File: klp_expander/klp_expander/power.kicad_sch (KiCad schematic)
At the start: 20 parts, among them U2 LM22678TJ-5, U4 AMS1117-3.3

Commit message: update schematics
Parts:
- added C40, C41: 100n, Capacitor_SMD:C_0402_1005Metric, symbol Device:C_Small
- added C46: 470p, Capacitor_SMD:C_0603_1608Metric, symbol Device:C
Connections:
- net +24V: now also C40.2, C41.2
- net GND: now also C40.1, C41.1, C46.1
- new net GNDS: C46.2

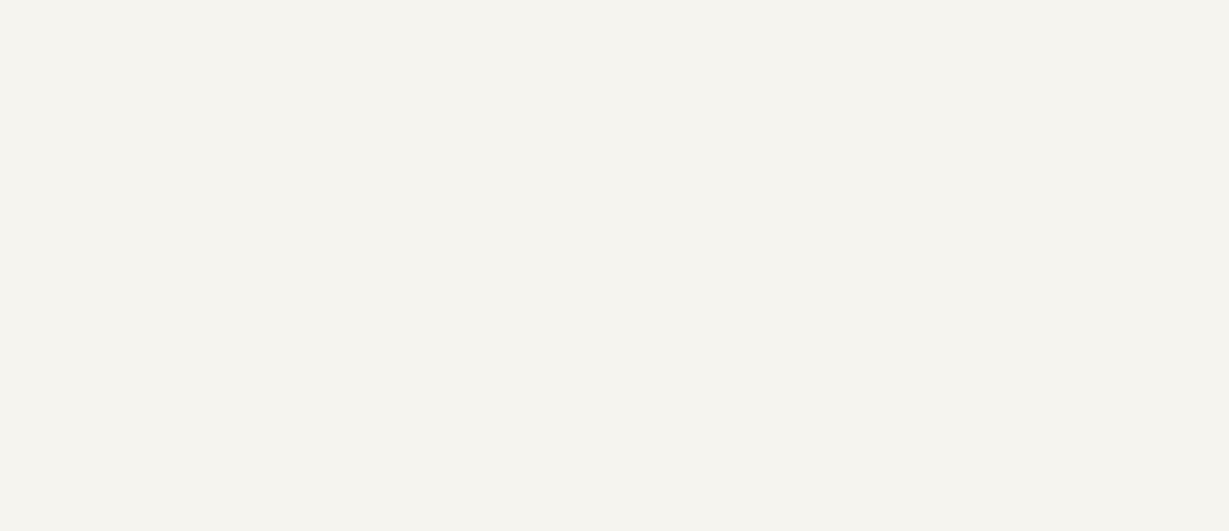
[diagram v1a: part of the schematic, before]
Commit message: feat: merge middle mcu into klp expander. both projects will be merged and will get a new name
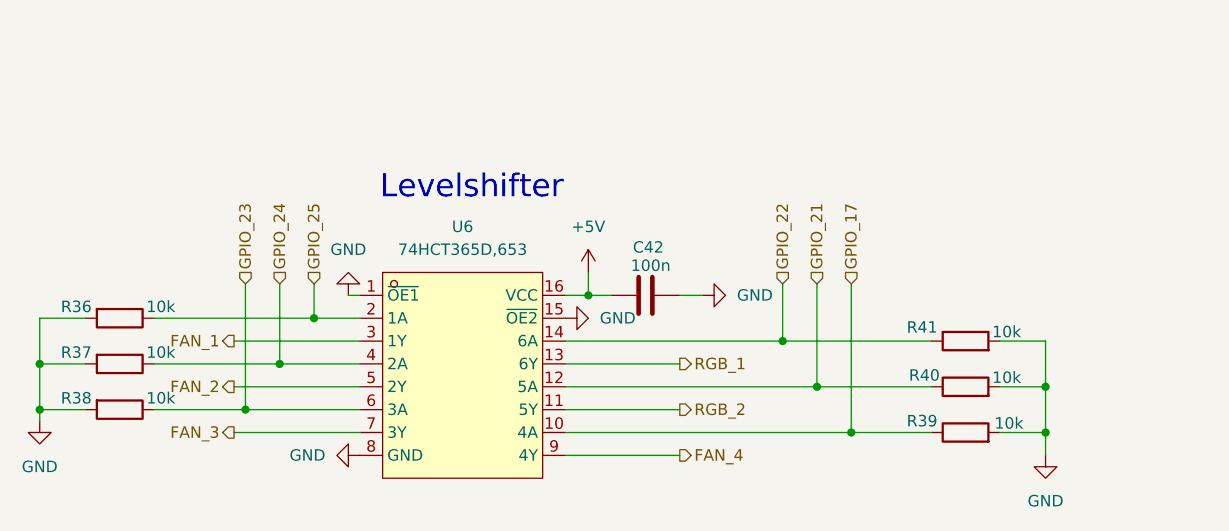
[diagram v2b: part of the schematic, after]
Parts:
- added C42: 100n, Capacitor_SMD:C_0402_1005Metric, symbol Device:C
- added R36, R37, R38, R39, R40, R41: 10k, Resistor_SMD:R_0402_1005Metric, symbol Device:R
- added U6: 74HCT365D,653, :SOP-16_L10.0-W3.9-P1.27-LS6.0-BL, symbol LCSC:74HCT365D,653
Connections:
- net +5V: now also C42.1, U6.16 (VCC)
- net GND: now also C42.2, R36.2, R37.2, R38.2, R39.2, R40.2, R41.2, U6.1 (~{OE1}), U6.15 (~{OE2}), U6.8 (GND)
- new net FAN_1: U6.3 (1Y)
- new net FAN_2: U6.5 (2Y)
- new net FAN_3: U6.7 (3Y)
- new net FAN_4: U6.9 (4Y)
- new net GPIO_17: R39.1, U6.10 (4A)
- new net GPIO_21: R40.1, U6.12 (5A)
- new net GPIO_22: R41.1, U6.14 (6A)
- new net GPIO_23: R38.1, U6.6 (3A)
- new net GPIO_24: R37.1, U6.4 (2A)
- new net GPIO_25: R36.1, U6.2 (1A)
- new net RGB_1: U6.13 (6Y)
- new net RGB_2: U6.11 (5Y)
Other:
- note added: "Levelshifter"
